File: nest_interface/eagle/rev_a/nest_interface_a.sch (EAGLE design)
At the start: 87 parts, among them J1 MOLEX_MICRO_USB_B_047346, J10 CONN_BLOCK_2, J11 CONN_BLOCK_2, J12 CONN_BLOCK_2, J13 CONN_BLOCK_2, J14 CONN_BLOCK_2, J15 CONN_BLOCK_2, J2 CONN_BLOCK_2, J3 CONN_BLOCK_3, J4 PJ-036A-SMT, J5 CONN_BLOCK_3, J6 CONN_BLOCK_3, J7 CONN_BLOCK_2, J8 CONN_BLOCK_3, J9 CONN_BLOCK_3, U1 FT232RL, U2 EPIC-CORE_A

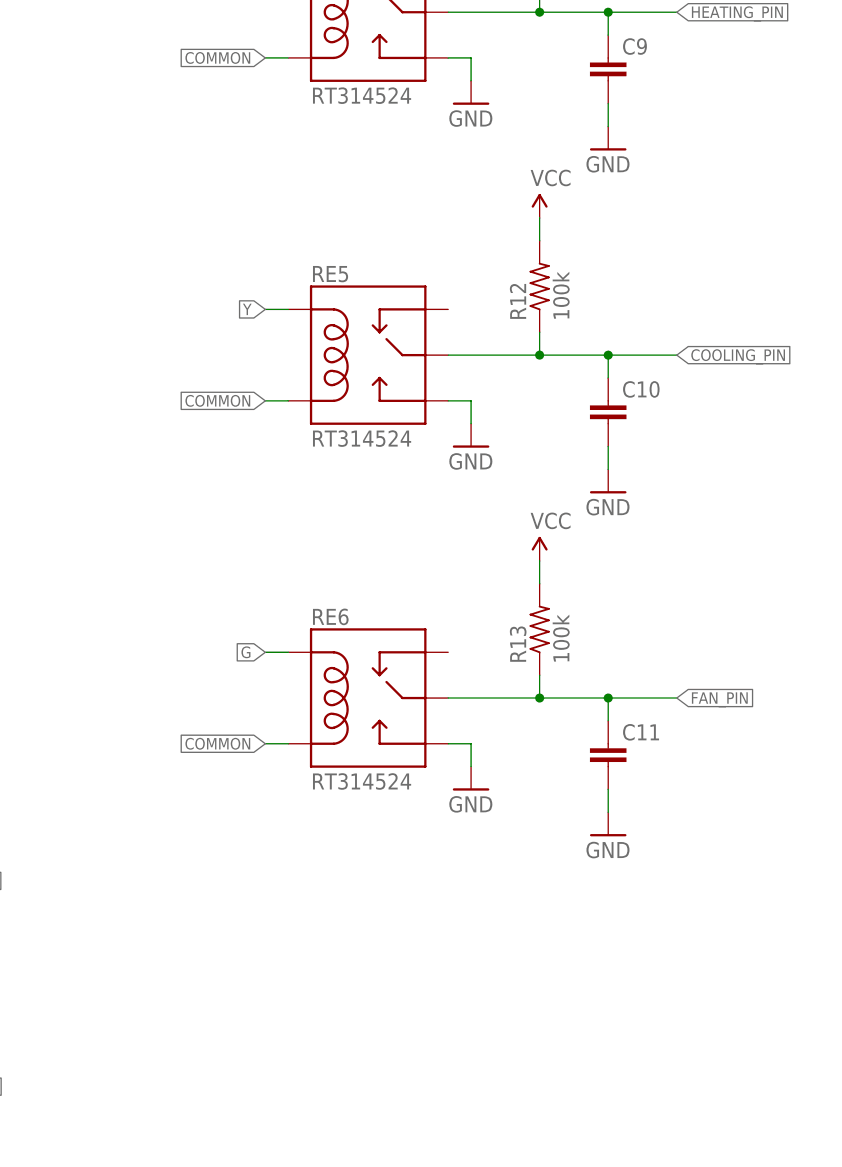
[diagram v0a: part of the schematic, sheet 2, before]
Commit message: started routing the nest interface board
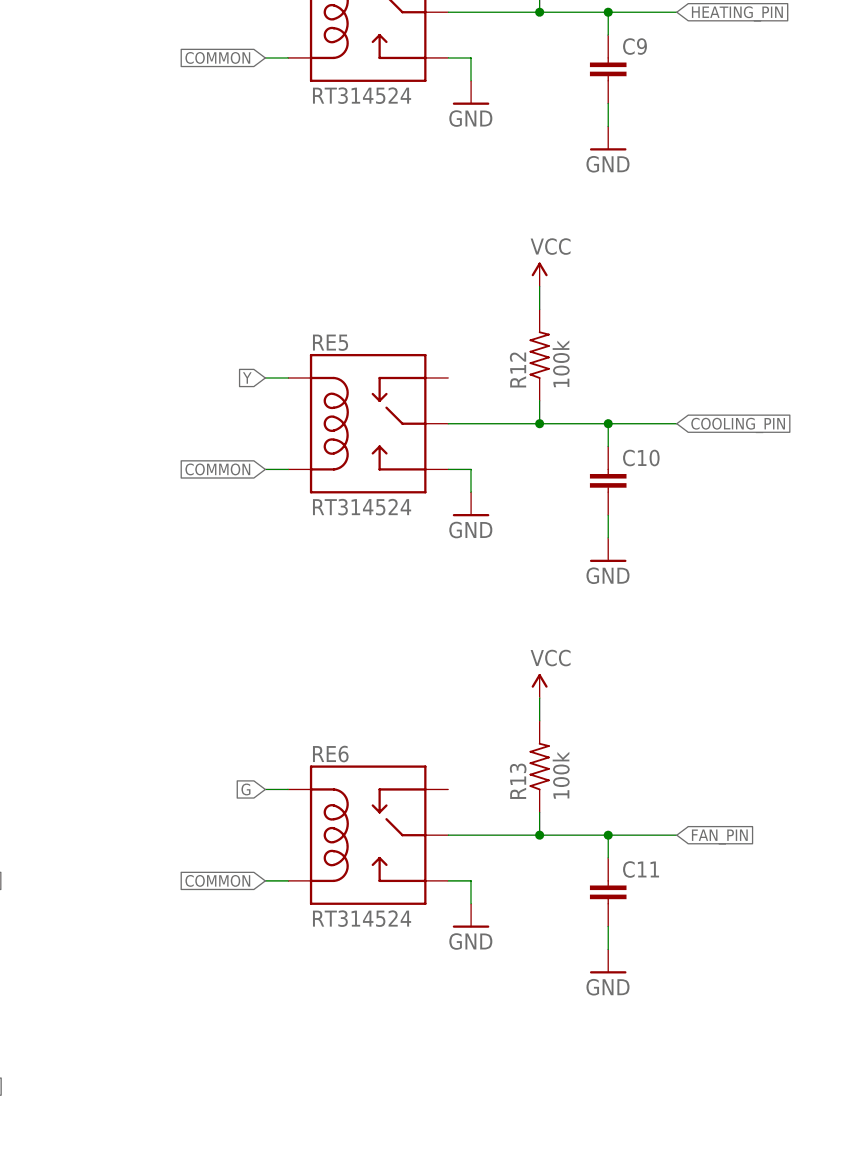
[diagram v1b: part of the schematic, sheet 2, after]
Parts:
- added JP1: (no value), pinhead:PINHD-2X10
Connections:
- new net ADC5: JP1.1, U2.ADC5
- new net ADC6/DAC0: JP1.3, U2.ADC6/DAC0
- new net ADC7/DAC1: JP1.5, U2.ADC7/DAC1
- new net MISO0: JP1.11, U2.MISO0
- new net MOSI0/SDA: JP1.9, U2.MOSI0/SDA
- new net P2.0: JP1.2, U2.P2.0
- new net P2.1: JP1.4, U2.P2.1
- new net P2.3: JP1.6, U2.P2.3
- new net P2.6: JP1.8, U2.P2.6
- new net RADIO_SFD: JP1.10, U2.RADIO_SFD
- new net SCLK0/SCL: JP1.13, U2.SCLK0/SCL
- new net STE0: JP1.7, U2.STE0
- new net UART0RX: JP1.17, U2.UART0RX
- new net UART0TX: JP1.15, U2.UART0TX
- net FAN_PIN: now also U2.P1.5; no longer U2.P1.7
- net HEATING_PIN: now also U2.P1.7; no longer U2.P1.5
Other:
- moved on the sheet: C10, C11, C5, R12, R13, RE5, RE6

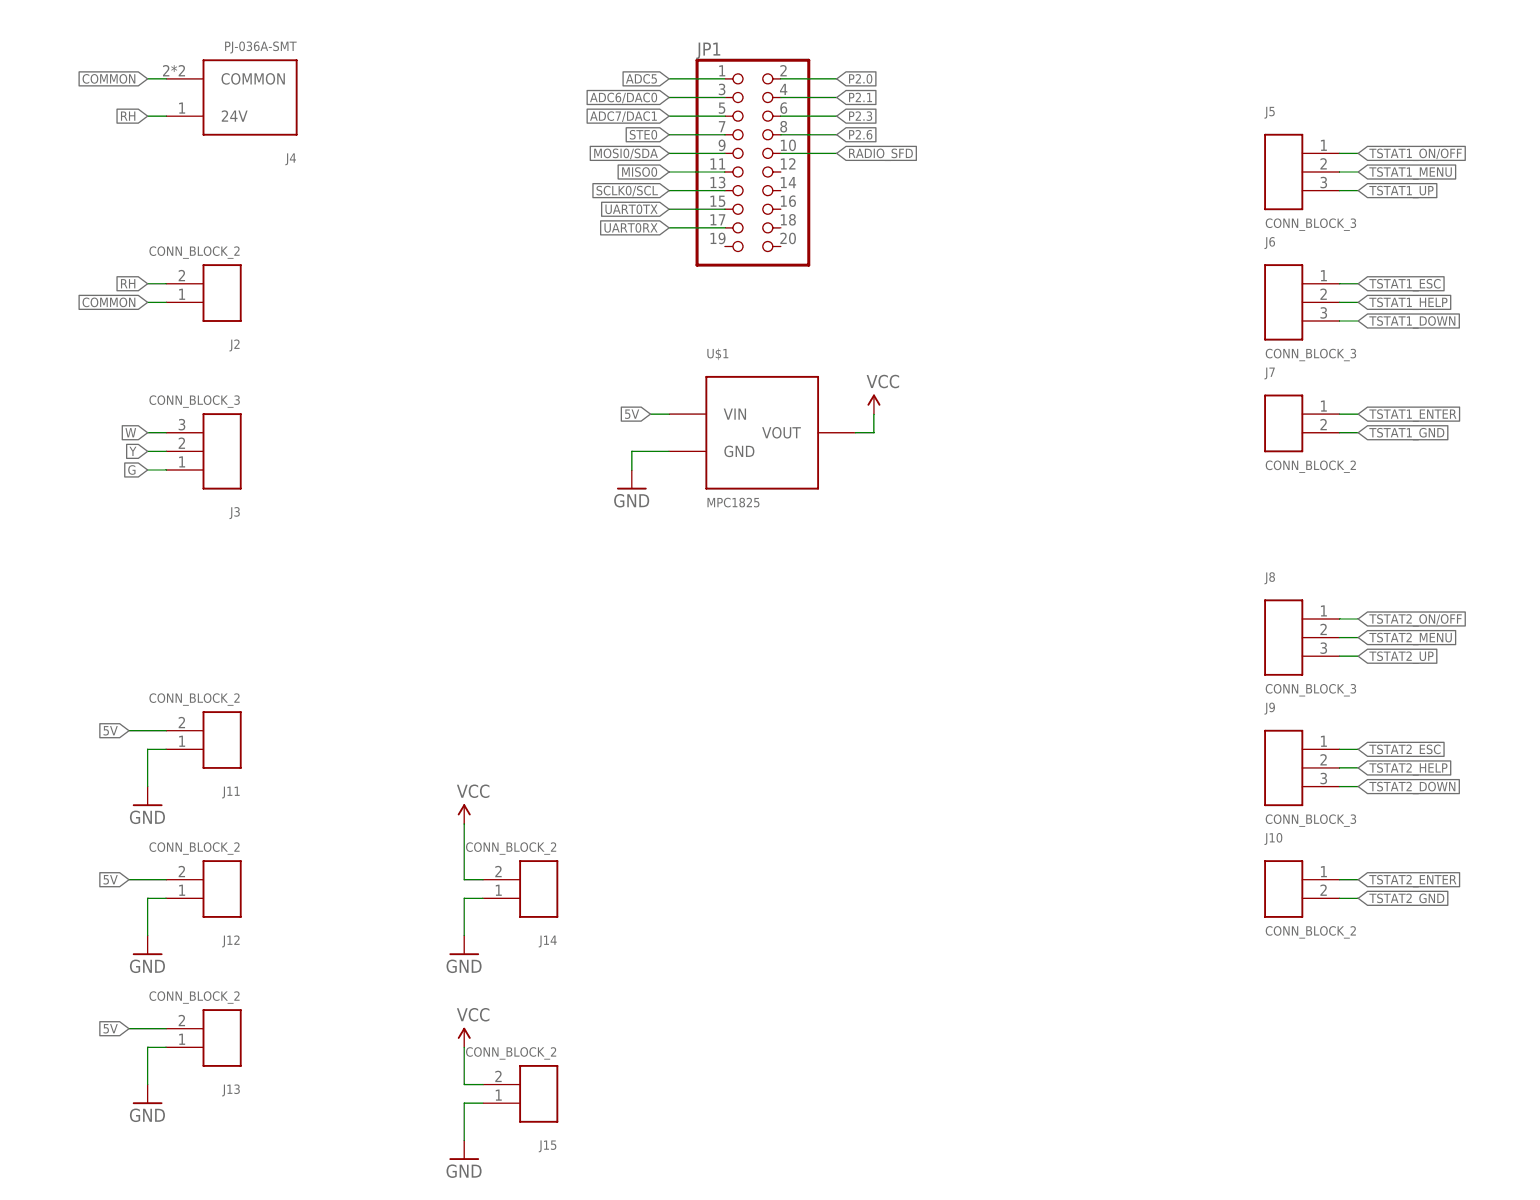
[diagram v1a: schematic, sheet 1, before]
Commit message: routed the nest interface board
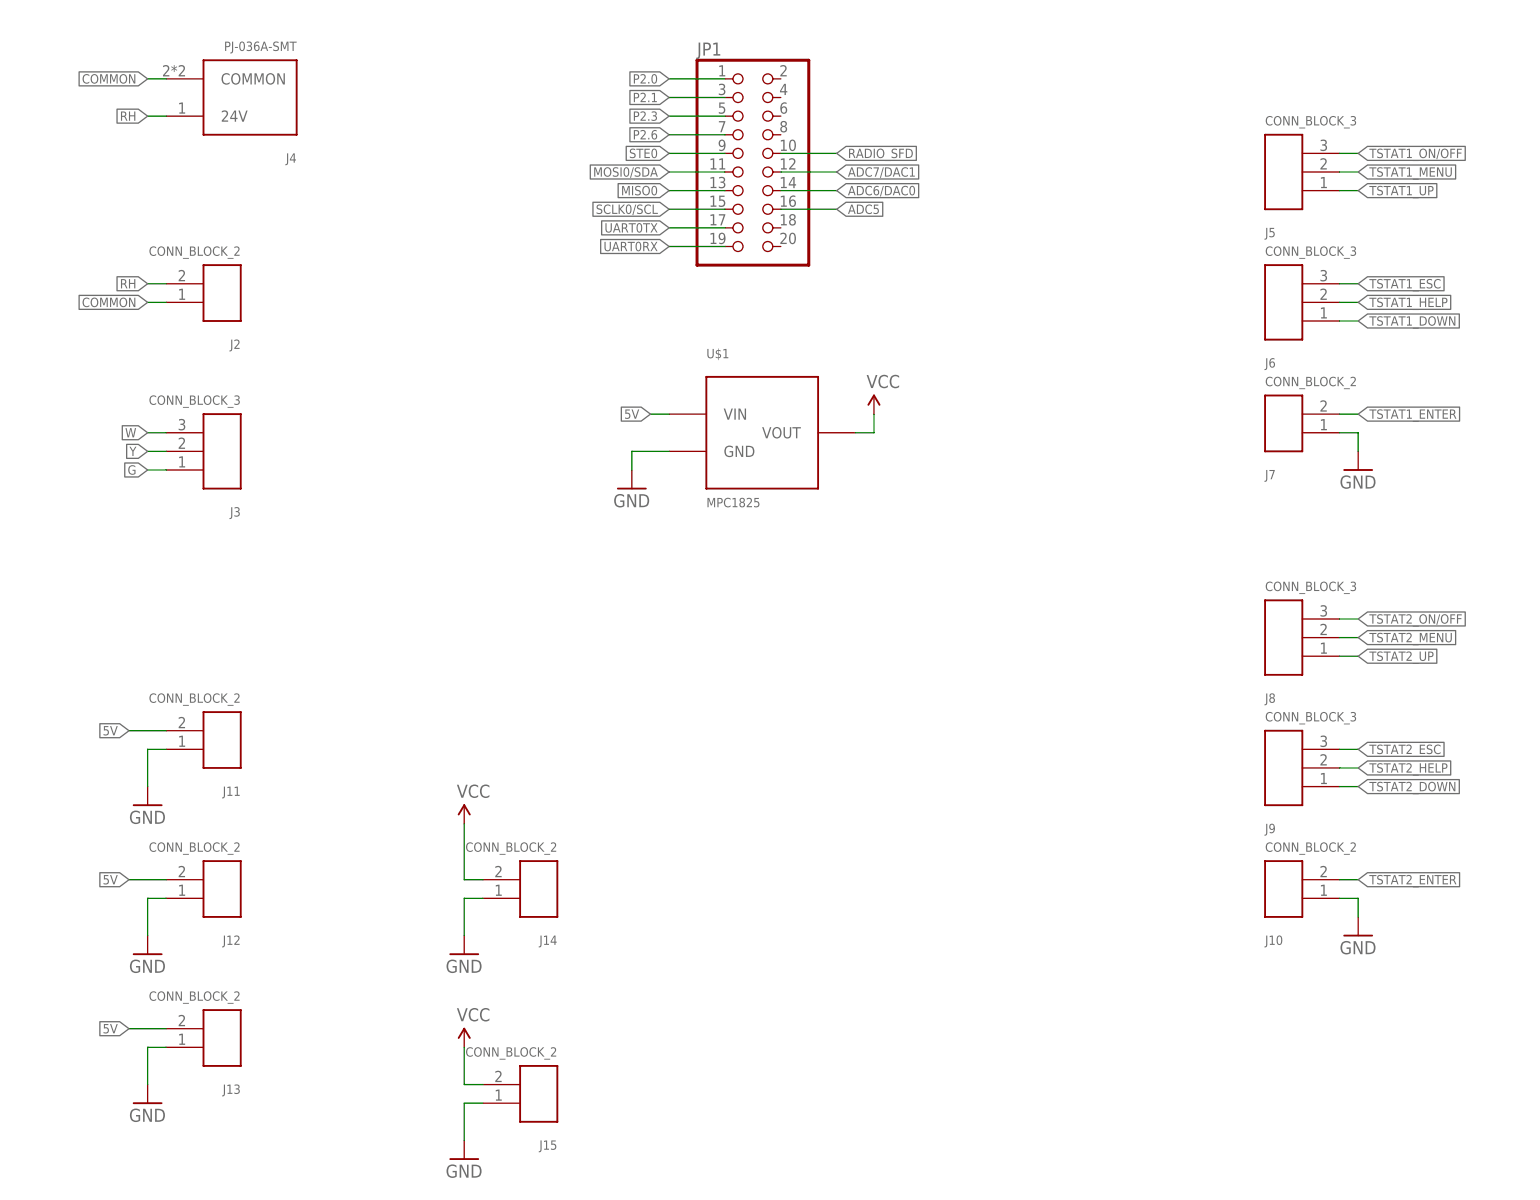
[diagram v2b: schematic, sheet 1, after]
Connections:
- removed net TSTAT1_GND: J7.2
- removed net TSTAT2_GND: J10.2
- net ADC5: now also JP1.16; no longer JP1.1
- net ADC6/DAC0: now also JP1.14; no longer JP1.3
- net ADC7/DAC1: now also JP1.12; no longer JP1.5
- net GND: now also J10.1, J7.1
- net MISO0: now also JP1.13; no longer JP1.11
- net MOSI0/SDA: now also JP1.11; no longer JP1.9
- net P2.0: now also JP1.1; no longer JP1.2
- net P2.1: now also JP1.3; no longer JP1.4
- net P2.3: now also JP1.5; no longer JP1.6
- net P2.6: now also JP1.7; no longer JP1.8
- net SCLK0/SCL: now also JP1.15; no longer JP1.13
- net STE0: now also JP1.9; no longer JP1.7
- net TSTAT1_DOWN: now also J6.1; no longer J6.3
- net TSTAT1_DOWN_PIN: now also U2.P5.2; no longer U2.P5.5
- net TSTAT1_ENTER: now also J7.2; no longer J7.1
- net TSTAT1_ENTER_PIN: now also U2.P5.1; no longer U2.P5.6
- net TSTAT1_ESC: now also J6.3; no longer J6.1
- net TSTAT1_ESC_PIN: now also U2.P5.4; no longer U2.P5.3
- net TSTAT1_HELP_PIN: now also U2.P5.3; no longer U2.P5.4
- net TSTAT1_MENU_PIN: now also U2.P5.6; no longer U2.P5.1
- net TSTAT1_ON/OFF: now also J5.3; no longer J5.1
- net TSTAT1_ON/OFF_PIN: now also U2.P5.7; no longer U2.P5.0
- net TSTAT1_UP: now also J5.1; no longer J5.3
- net TSTAT1_UP_PIN: now also U2.P5.5; no longer U2.P5.2
- net TSTAT2_DOWN: now also J9.1; no longer J9.3
- net TSTAT2_ENTER: now also J10.2; no longer J10.1
- net TSTAT2_ESC: now also J9.3; no longer J9.1
- net TSTAT2_ON/OFF: now also J8.3; no longer J8.1
- net TSTAT2_ON/OFF_PIN: now also U2.P5.0; no longer U2.P5.7
- net TSTAT2_UP: now also J8.1; no longer J8.3
- net UART0RX: now also JP1.19; no longer JP1.17
- net UART0TX: now also JP1.17; no longer JP1.15
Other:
- moved on the sheet: J10, J5, J6, J7, J8, J9

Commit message: added silkscreen to nest board
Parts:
- removed S1: (no value), SparkFun:SWITCH-SPSTPTH
- added J16: CONN_BLOCK_2, nest_interface:CONN_BLOCK_2
- R10, R14, R6, R8: value 10k -> 100k
- R11, R13, R15, R9: value 100k -> 10k
- renumbered RE4 to RE1, RE5 to RE2, RE6 to RE3, U$1 to U3
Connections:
- removed net N$13: S1.P, U1.!RTS
- removed net N$8: S1.O, S2.P$2, S2.P$4, U2.RST/NMI
- new net RST: J16.1, S2.P$2, S2.P$4, U2.RST/NMI
- new net RST_USB: J16.2, U1.!RTS
- net COMMON: now also J2.2; no longer J2.1
- net COOLING_PIN: now also R7.1; no longer R12.1
- net FAN_PIN: now also R8.1; no longer R13.1
- net GND: now also JP1.20, R10.2, R12.2, R14.2; no longer R15.2, R7.2, R9.2
- net HEATING_PIN: now also R6.1; no longer R11.1
- net N$16: now also Q2.B, R11.1; no longer Q1.B, R6.1
- net N$17: now also Q1.B, R9.1; no longer Q2.B, R14.1
- net N$25: now also R13.1; no longer R8.1
- net N$26: now also R15.1; no longer R10.1
- net RH: now also J2.1; no longer J2.2
- net TSTAT1_ESC_PIN: now also R15.2; no longer R10.2
- net TSTAT1_MENU: now also Q2.C; no longer Q1.C
- net TSTAT1_MENU_PIN: now also R11.2, R12.1; no longer R6.2, R7.1
- net TSTAT1_ON/OFF: now also Q1.C; no longer Q2.C
- net TSTAT1_ON/OFF_PIN: now also R10.1, R9.2; no longer R14.2, R15.1
- net TSTAT1_UP_PIN: now also R13.2, R14.1; no longer R8.2, R9.1
- net VCC: now also JP1.2, R6.2, R7.2, R8.2; no longer R11.2, R12.2, R13.2
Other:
- moved on the sheet: Q1, Q2, R10, R11, R12, R13, R14, R15, R6, R7, R8, R9

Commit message: adding more relays to the nest interface board in
prep for v2
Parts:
- added C6, C7, C8: (no value), rcl:C-EUC0603
- added J17: CONN_BLOCK_3, nest_interface:CONN_BLOCK_3
- added R37, R38, R39: 100k, rcl:R-US_R0603
- added RE4, RE5, RE6: RT314524, nest_interface:RT314524
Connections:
- net COOLING_PIN renamed COOLING1_PIN
- net HEATING_PIN renamed HEATING1_PIN
- net W renamed W1
- net Y renamed Y1
- new net COOLING2_PIN: C7.1, R38.1, RE5.MAIN
- new net HEATING2_PIN: C6.1, R37.1, RE4.MAIN
- new net STAR: J17.1, RE6.COIL1
- new net STAR_PIN: C8.1, R39.1, RE6.MAIN
- new net W2: J17.3, RE4.COIL1
- new net Y2: J17.2, RE5.COIL1
- net COMMON: now also RE4.COIL2, RE5.COIL2, RE6.COIL2
- net GND: now also C6.2, C7.2, C8.2, RE4.NO, RE5.NO, RE6.NO
- net VCC: now also R37.2, R38.2, R39.2
